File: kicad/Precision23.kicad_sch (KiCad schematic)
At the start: 27 parts, among them J396 STANDOFF, J397 STANDOFF, J398 STANDOFF, J399 STANDOFF, J503 Conn_02x03_Odd_Even, J504 Conn_01x06, J505 Conn_01x06, J506 Conn_01x05, J507 Conn_01x05, J508 Conn_01x06, J509 Conn_01x02_Pin, J596 STANDOFF, J597 STANDOFF, J598 STANDOFF, J599 STANDOFF, U501 SAM-M8Q, U502 NC7SZ157, U503 NC7SZ157, U504 NC7SZ157

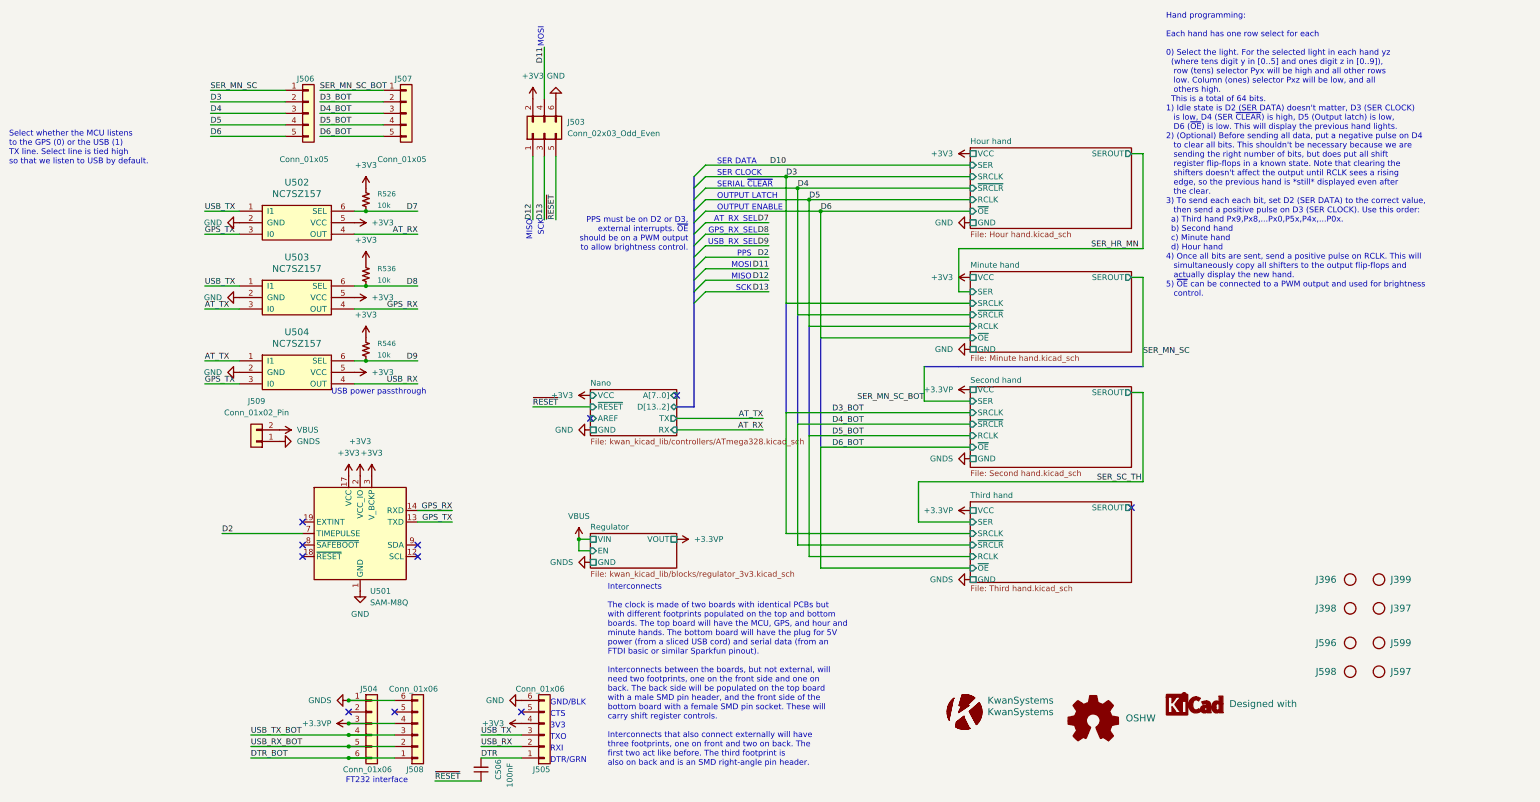
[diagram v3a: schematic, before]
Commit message: Reorganize and finish routing. This will work for 3V3 but might not be as bright as possible.
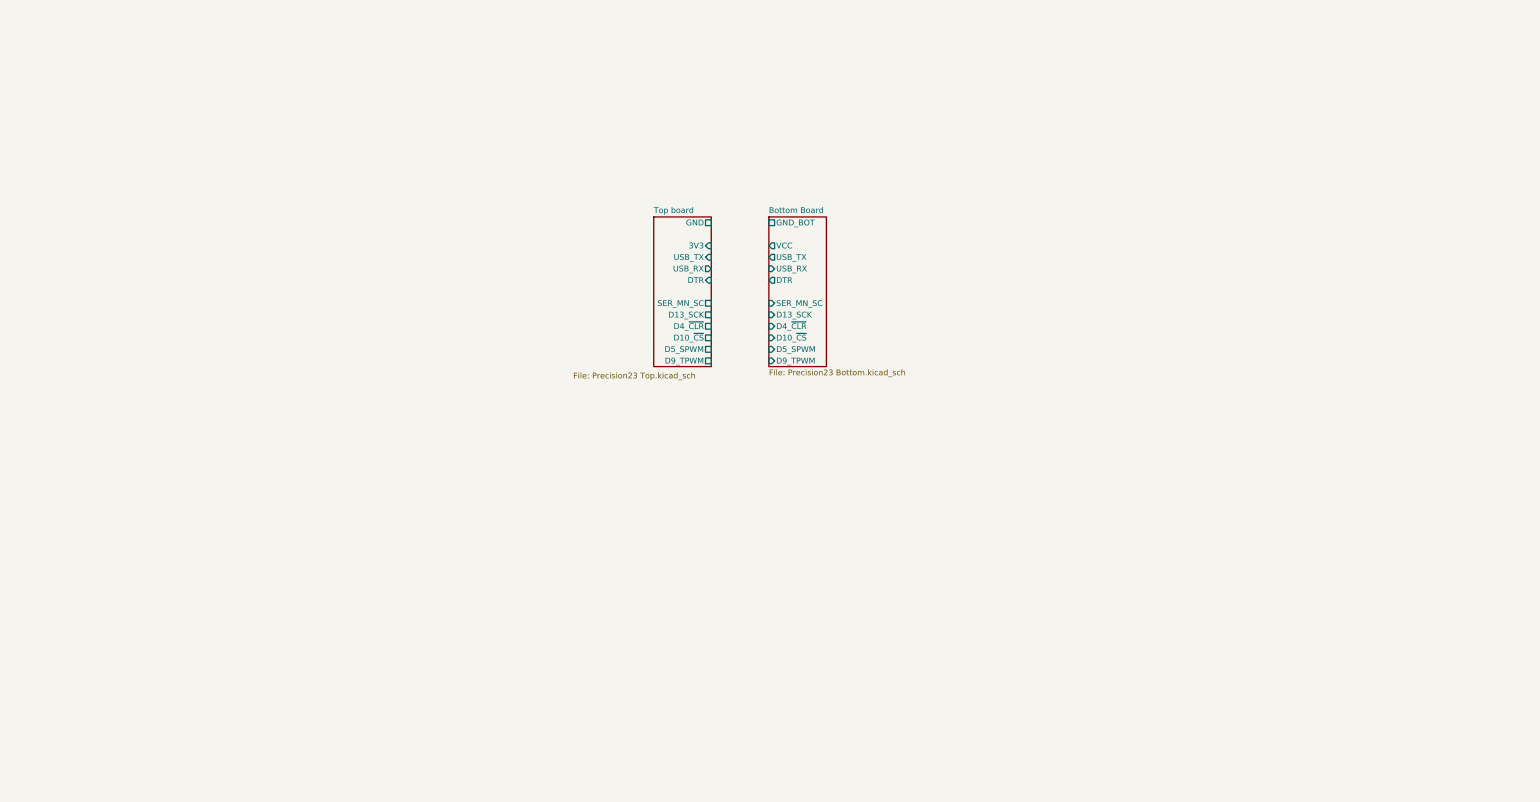
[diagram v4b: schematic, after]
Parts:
- removed C506: 100nF, Capacitor_SMD:C_0603_1608Metric, symbol Device:C_Small
- removed G101: KwanSystems, KwanSystems:PrecisionKwan, symbol KwanSystems:KwanSystems
- removed G102: KwanSystems, KwanSystems:StKwansSoldermask, symbol KwanSystems:KwanSystems
- removed G301: OSHW, KwanSystems:OSHW-Symbol_6.7x6mm_SolderMask, symbol KwanSystems:OSHW
- removed G302: Designed with, KwanSystems:Symbol_KiCAD-Logo_CopperAndSilkScreenTop_small, symbol KwanSystems:DesignedWithKicad
- removed J396, J397, J398, J399, J596, J597, J598, J599: STANDOFF, KwanSystems:STANDOFF_NONPLATED, symbol KwanSystems:STANDOFF
- removed J503: Conn_02x03_Odd_Even, Connector_PinHeader_2.54mm:PinHeader_2x03_P2.54mm_Vertical_SMD, symbol Connector_Generic:Conn_02x03_Odd_Even
- removed J504: Conn_01x06, KwanSystems:SAMTEC_TSM-106-01-T-SH, symbol Connector_Generic:Conn_01x06
- removed J505: Conn_01x06, Connector_PinHeader_2.54mm:PinHeader_1x06_P2.54mm_Vertical_SMD_Pin1Left, symbol Connector_Generic:Conn_01x06
- removed J506: Conn_01x05, Connector_PinHeader_2.54mm:PinHeader_1x05_P2.54mm_Vertical_SMD_Pin1Left, symbol Connector_Generic:Conn_01x05
- removed J507: Conn_01x05, Connector_PinSocket_2.54mm:PinSocket_1x05_P2.54mm_Vertical_SMD_Pin1Left, symbol Connector_Generic:Conn_01x05
- removed J508: Conn_01x06, Connector_PinSocket_2.54mm:PinSocket_1x06_P2.54mm_Vertical_SMD_Pin1Left, symbol Connector_Generic:Conn_01x06
- removed J509: Conn_01x02_Pin, KwanSystems:SAMTEC_TSM-102-01-T-SH, symbol Connector_Generic:Conn_01x02
- removed R526, R536, R546: 10k, Resistor_SMD:R_0603_1608Metric, symbol KwanSystems:RESISTOR
- removed U501: SAM-M8Q, RF_GPS:ublox_SAM-M8Q, symbol RF_GPS:SAM-M8Q
- removed U502, U503, U504: NC7SZ157, Package_TO_SOT_SMD:SOT-363_SC-70-6, symbol KwanSystems:NC7SZ157
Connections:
- no-connect marks 11 -> 0
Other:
- removed sheet Hour hand
- removed sheet Minute hand
- removed sheet Nano
- removed sheet Regulator
- removed sheet Second hand
- removed sheet Third hand
- added sheet Bottom Board (Precision23 Bottom.kicad_sch)
- added sheet Top board (Precision23 Top.kicad_sch)
- note removed: "3V3"
- note removed: "AT_RX_SEL"
- note removed: "CTS"
- note removed: "DTR/GRN"
- note removed: "FT232 interface"
- note removed: "GND/BLK"
- note removed: "GPS_RX_SEL"
- note removed: "Hand programming: Each hand has one row select for each 0) Select the light. For the selected light in each hand yz (where tens digit y in [0..5] and ones digit z in [0..9]), row (tens) selector Pyx will be high and all other rows low. Column (ones) selector Pxz will be low, and all others high. This is a total of 64 bits. 1) Idle state is D2 (SER DATA) doesn't matter, D3 (SER CLOCK) is low, D4 (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"
- note removed: "Interconnects The clock is made of two boards with identical PCBs but with different footprints populated on the top and bottom boards. The top board will have the MCU, GPS, and hour and minute hands. The bottom board will have the plug for 5V power (from a sliced USB cord) and serial data (from an FTDI basic or similar Sparkfun pinout). Interconnects between the boards, but not external, will ne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"
- note removed: "MISO"
- note removed: "MOSI"
- note removed: "OUTPUT ENABLE"
- note removed: "OUTPUT LATCH"
- note removed: "PPS"
- note removed: "PPS must be on D2 or D3, external interrupts. ~{OE} should be on a PWM output to allow brightness control."
- note removed: "RXI"
- note removed: "SCK"
- note removed: "SER CLOCK"
- note removed: "SER DATA"
- note removed: "SERIAL ~{CLEAR}"
- note removed: "Select whether the MCU listens to the GPS (0) or the USB (1) TX line. Select line is tied high so that we listen to USB by default."
- note removed: "TXO"
- note removed: "USB power passthrough"
- note removed: "USB_RX_SEL"

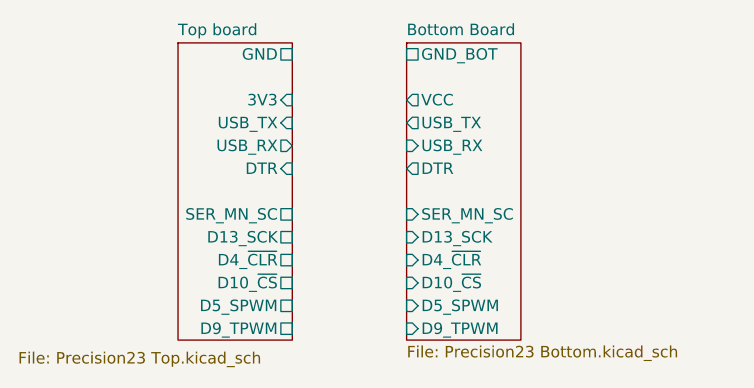
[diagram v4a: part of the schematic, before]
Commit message: Refactored board, put 5V0 on all parts except GPS
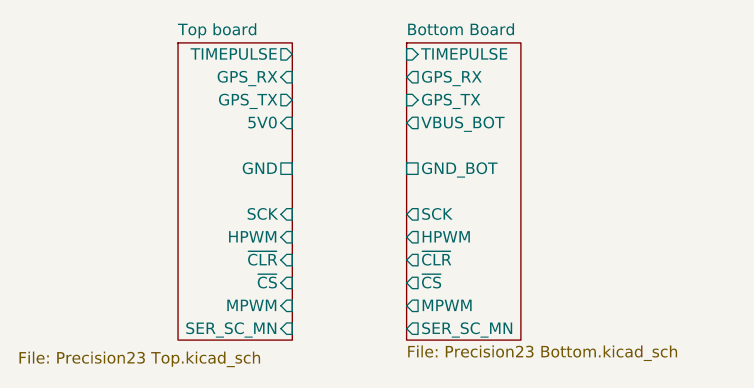
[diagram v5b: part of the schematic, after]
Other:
- sheet Bottom Board ports: added GPS_RX, GPS_TX, HPWM, MPWM, SCK, SER_SC_MN, TIMEPULSE, VBUS_BOT, ~{CLR}, ~{CS}; removed D10_~{CS}, D13_SCK, D4_~{CLR}, D5_SPWM, D9_TPWM, DTR, SER_MN_SC, USB_RX, USB_TX, VCC
- sheet Top board ports: added 5V0, GPS_RX, GPS_TX, HPWM, MPWM, SCK, SER_SC_MN, TIMEPULSE, ~{CLR}, ~{CS}; removed 3V3, D10_~{CS}, D13_SCK, D4_~{CLR}, D5_SPWM, D9_TPWM, DTR, SER_MN_SC, USB_RX, USB_TX
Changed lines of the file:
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@@
       (effects (font (size 1.27 1.27)) (justify left top))
     )
-    (pin "D10_~{CS}" passive (at 127 88.9 0)
+    (pin "5V0" input (at 127 71.12 0)
       (effects (font (size 1.27 1.27)) (justify right))
     )
-    (pin "SER_MN_SC" passive (at 127 81.28 0)
+    (pin "GPS_RX" input (at 127 66.04 0)
       (effects (font (size 1.27 1.27)) (justify right))
     )
-    (pin "USB_RX" output (at 127 73.66 0)
+    (pin "GPS_TX" output (at 127 68.58 0)
       (effects (font (size 1.27 1.27)) (justify right))
     )
-    (pin "D13_SCK" passive (at 127 83.82 0)
+    (pin "TIMEPULSE" output (at 127 63.5 0)
       (effects (font (size 1.27 1.27)) (justify right))
     )
-    (pin "D4_~{CLR}" passive (at 127 86.36 0)
+    (pin "GND" passive (at 127 76.2 0)
       (effects (font (size 1.27 1.27)) (justify right))
     )
-    (pin "GND" passive (at 127 63.5 0)
+    (pin "~{CLR}" input (at 127 86.36 0)
       (effects (font (size 1.27 1.27)) (justify right))
     )
-    (pin "3V3" input (at 127 68.58 0)
+    (pin "SER_SC_MN" input (at 127 93.98 0)
       (effects (font (size 1.27 1.27)) (justify right))
     )
-    (pin "USB_TX" input (at 127 71.12 0)
+    (pin "MPWM" input (at 127 91.44 0)
       (effects (font (size 1.27 1.27)) (justify right))
     )
-    (pin "DTR" input (at 127 76.2 0)
+    (pin "~{CS}" input (at 127 88.9 0)
       (effects (font (size 1.27 1.27)) (justify right))
     )
-    (pin "D5_SPWM" passive (at 127 91.44 0)
+    (pin "HPWM" input (at 127 83.82 0)
       (effects (font (size 1.27 1.27)) (justify right))
     )
-    (pin "D9_TPWM" passive (at 127 93.98 0)
+    (pin "SCK" input (at 127 81.28 0)
       (effects (font (size 1.27 1.27)) (justify right))
     )
@@
       (effects (font (size 1.27 1.27)) (justify left top))
     )
-    (pin "USB_RX" input (at 139.7 73.66 180)
+    (pin "SCK" output (at 139.7 81.28 180)
       (effects (font (size 1.27 1.27)) (justify left))
     )
-    (pin "D5_SPWM" input (at 139.7 91.44 180)
+    (pin "SER_SC_MN" output (at 139.7 93.98 180)
       (effects (font (size 1.27 1.27)) (justify left))
     )
-    (pin "SER_MN_SC" input (at 139.7 81.28 180)
+    (pin "HPWM" output (at 139.7 83.82 180)
       (effects (font (size 1.27 1.27)) (justify left))
     )
-    (pin "D13_SCK" input (at 139.7 83.82 180)
+    (pin "~{CLR}" output (at 139.7 86.36 180)
       (effects (font (size 1.27 1.27)) (justify left))
     )
-    (pin "D9_TPWM" input (at 139.7 93.98 180)
+    (pin "~{CS}" output (at 139.7 88.9 180)
       (effects (font (size 1.27 1.27)) (justify left))
     )
-    (pin "USB_TX" output (at 139.7 71.12 180)
+    (pin "MPWM" output (at 139.7 91.44 180)
       (effects (font (size 1.27 1.27)) (justify left))
     )
-    (pin "VCC" output (at 139.7 68.58 180)
+    (pin "GND_BOT" passive (at 139.7 76.2 180)
       (effects (font (size 1.27 1.27)) (justify left))
     )
-    (pin "DTR" output (at 139.7 76.2 180)
+    (pin "GPS_RX" output (at 139.7 66.04 180)
       (effects (font (size 1.27 1.27)) (justify left))
     )
-    (pin "D4_~{CLR}" input (at 139.7 86.36 180)
+    (pin "GPS_TX" input (at 139.7 68.58 180)
       (effects (font (size 1.27 1.27)) (justify left))
     )
-    (pin "D10_~{CS}" input (at 139.7 88.9 180)
+    (pin "VBUS_BOT" output (at 139.7 71.12 180)
       (effects (font (size 1.27 1.27)) (justify left))
     )
-    (pin "GND_BOT" passive (at 139.7 63.5 180)
+    (pin "TIMEPULSE" input (at 139.7 63.5 180)
       (effects (font (size 1.27 1.27)) (justify left))
     )

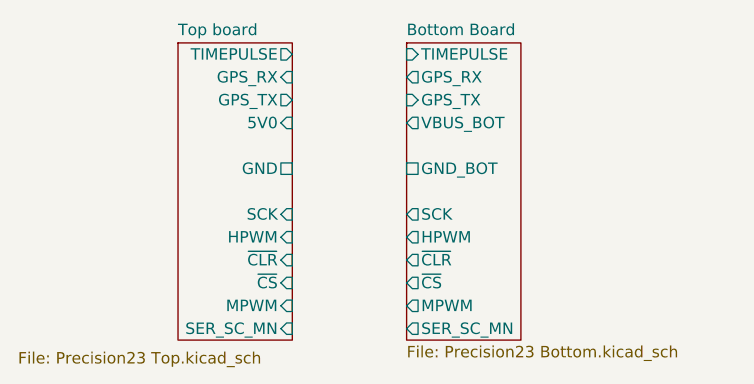
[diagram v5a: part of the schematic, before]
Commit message: Put MOSFET switch transistors in place. We won't end up using these.
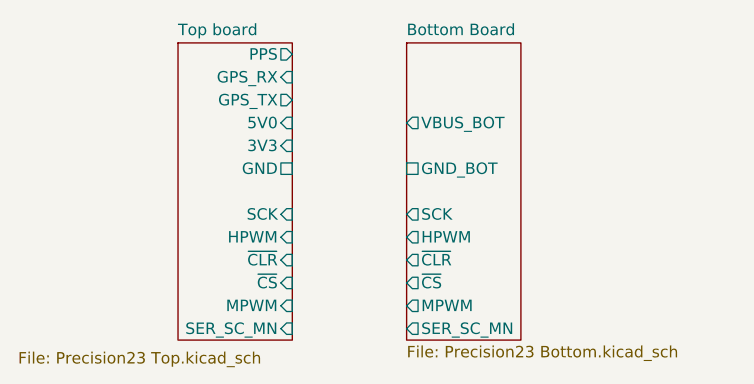
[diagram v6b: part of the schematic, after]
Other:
- sheet Bottom Board ports: added none; removed GPS_RX, GPS_TX, TIMEPULSE
- sheet Top board ports: added 3V3, PPS; removed TIMEPULSE
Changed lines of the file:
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@@
       (effects (font (size 1.27 1.27)) (justify left top))
-    )
-    (pin "5V0" input (at 127 71.12 0)
-      (effects (font (size 1.27 1.27)) (justify right))
-    )
-    (pin "GPS_RX" input (at 127 66.04 0)
-      (effects (font (size 1.27 1.27)) (justify right))
-    )
-    (pin "GPS_TX" output (at 127 68.58 0)
-      (effects (font (size 1.27 1.27)) (justify right))
-    )
-    (pin "TIMEPULSE" output (at 127 63.5 0)
-      (effects (font (size 1.27 1.27)) (justify right))
-    )
-    (pin "GND" passive (at 127 76.2 0)
-      (effects (font (size 1.27 1.27)) (justify right))
     )
     (pin "~{CLR}" input (at 127 86.36 0)
@@
     )
     (pin "SCK" input (at 127 81.28 0)
+      (effects (font (size 1.27 1.27)) (justify right))
+    )
+    (pin "PPS" output (at 127 63.5 0)
+      (effects (font (size 1.27 1.27)) (justify right))
+    )
+    (pin "GND" passive (at 127 76.2 0)
+      (effects (font (size 1.27 1.27)) (justify right))
+    )
+    (pin "5V0" input (at 127 71.12 0)
+      (effects (font (size 1.27 1.27)) (justify right))
+    )
+    (pin "3V3" input (at 127 73.66 0)
+      (effects (font (size 1.27 1.27)) (justify right))
+    )
+    (pin "GPS_TX" output (at 127 68.58 0)
+      (effects (font (size 1.27 1.27)) (justify right))
+    )
+    (pin "GPS_RX" input (at 127 66.04 0)
       (effects (font (size 1.27 1.27)) (justify right))
     )
@@
       (effects (font (size 1.27 1.27)) (justify left))
     )
-    (pin "GPS_RX" output (at 139.7 66.04 180)
-      (effects (font (size 1.27 1.27)) (justify left))
-    )
-    (pin "GPS_TX" input (at 139.7 68.58 180)
-      (effects (font (size 1.27 1.27)) (justify left))
-    )
     (pin "VBUS_BOT" output (at 139.7 71.12 180)
       (effects (font (size 1.27 1.27)) (justify left))
     )
-    (pin "TIMEPULSE" input (at 139.7 63.5 180)
-      (effects (font (size 1.27 1.27)) (justify left))
-    )

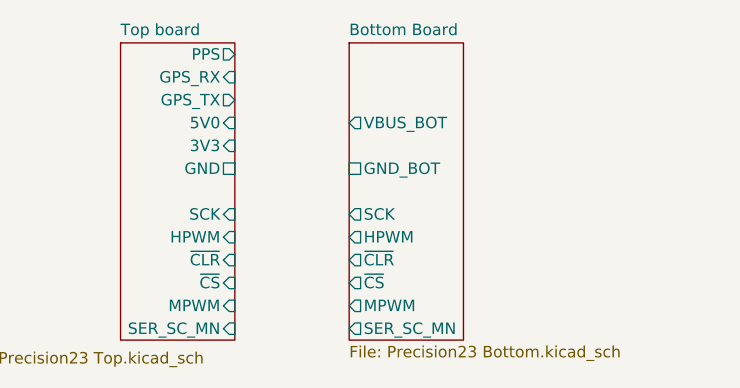
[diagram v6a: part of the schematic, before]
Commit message: Continue wiring MOSFET switches
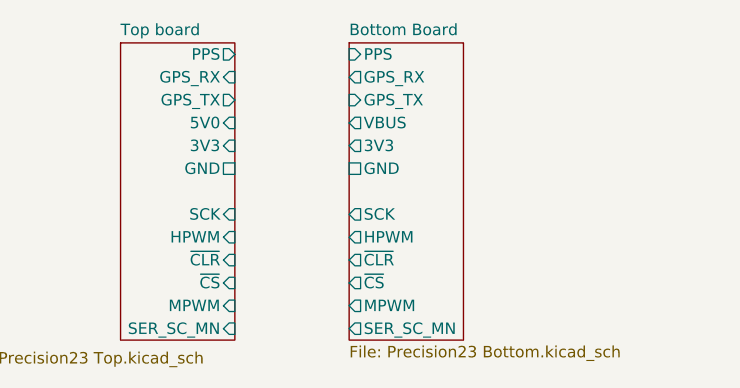
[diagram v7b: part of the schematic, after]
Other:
- sheet Bottom Board ports: added 3V3, GND, GPS_RX, GPS_TX, PPS, VBUS; removed GND_BOT, VBUS_BOT
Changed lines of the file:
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@@
       (effects (font (size 1.27 1.27)) (justify left))
     )
-    (pin "GND_BOT" passive (at 139.7 76.2 180)
+    (pin "PPS" input (at 139.7 63.5 180)
       (effects (font (size 1.27 1.27)) (justify left))
     )
-    (pin "VBUS_BOT" output (at 139.7 71.12 180)
+    (pin "GPS_RX" output (at 139.7 66.04 180)
       (effects (font (size 1.27 1.27)) (justify left))
     )
+    (pin "GPS_TX" input (at 139.7 68.58 180)
+      (effects (font (size 1.27 1.27)) (justify left))
+    )
+    (pin "3V3" output (at 139.7 73.66 180)
+      (effects (font (size 1.27 1.27)) (justify left))
+    )
+    (pin "VBUS" output (at 139.7 71.12 180)
+      (effects (font (size 1.27 1.27)) (justify left))
+    )
+    (pin "GND" passive (at 139.7 76.2 180)
+      (effects (font (size 1.27 1.27)) (justify left))
+    )

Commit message: Matrix8x8 stuff
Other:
- removed sheet Top board
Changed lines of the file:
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@@
 (kicad_sch (version 20230121) (generator eeschema)
   (paper "A4")
-  (sheet (at 114.3 62.23) (size 12.7 33.02)
-    (stroke (width 0.1524) (type solid))
-    (fill (color 0 0 0 0.0000))
-    (property "Sheetname" "Top board" (at 114.3 61.5184 0)
-      (effects (font (size 1.27 1.27)) (justify left bottom))
-    )
-    (property "Sheetfile" "Precision23 Top.kicad_sch" (at 96.52 96.52 0)
-      (effects (font (size 1.27 1.27)) (justify left top))
-    )
-    (pin "~{CLR}" input (at 127 86.36 0)
-      (effects (font (size 1.27 1.27)) (justify right))
-    )
-    (pin "SER_SC_MN" input (at 127 93.98 0)
-      (effects (font (size 1.27 1.27)) (justify right))
-    )
-    (pin "MPWM" input (at 127 91.44 0)
-      (effects (font (size 1.27 1.27)) (justify right))
-    )
-    (pin "~{CS}" input (at 127 88.9 0)
-      (effects (font (size 1.27 1.27)) (justify right))
-    )
-    (pin "HPWM" input (at 127 83.82 0)
-      (effects (font (size 1.27 1.27)) (justify right))
-    )
-    (pin "SCK" input (at 127 81.28 0)
-      (effects (font (size 1.27 1.27)) (justify right))
-    )
-    (pin "PPS" output (at 127 63.5 0)
-      (effects (font (size 1.27 1.27)) (justify right))
-    )
-    (pin "GND" passive (at 127 76.2 0)
-      (effects (font (size 1.27 1.27)) (justify right))
-    )
-    (pin "5V0" input (at 127 71.12 0)
-      (effects (font (size 1.27 1.27)) (justify right))
-    )
-    (pin "3V3" input (at 127 73.66 0)
-      (effects (font (size 1.27 1.27)) (justify right))
-    )
-    (pin "GPS_TX" output (at 127 68.58 0)
-      (effects (font (size 1.27 1.27)) (justify right))
-    )
-    (pin "GPS_RX" input (at 127 66.04 0)
-      (effects (font (size 1.27 1.27)) (justify right))
-    )
-    (instances
-      (project "Precision23"
-        (path "/9151f981-b383-4946-8df4-92ef46ef2206" (page "5"))
-      )
-    )
-  )
   (sheet (at 139.7 62.23) (size 12.7 33.02) (fields_autoplaced)
     (stroke (width 0.1524) (type solid))
